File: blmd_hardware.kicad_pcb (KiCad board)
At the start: 2 copper layers, 50 x 28.5 mm, 59 parts, among them J1 MR30PW-F, J2 control, J3 GND, J4 12V, J5 STLink-V3, Q1 RH6L040BG, Q2 RH6L040BG, Q3 RH6L040BG, Q4 RH6L040BG, Q5 RH6L040BG, Q6 RH6L040BG, SW1 reset, SW2 KHS42E, U1 A4939KLPTR-5-T, U10 STM32G431KBTx, U4 ISO7760FDBQR, U6 ACS711KEXLT-31AB, U7 ACS711KEXLT-31AB, U9 BD41041FJ-C

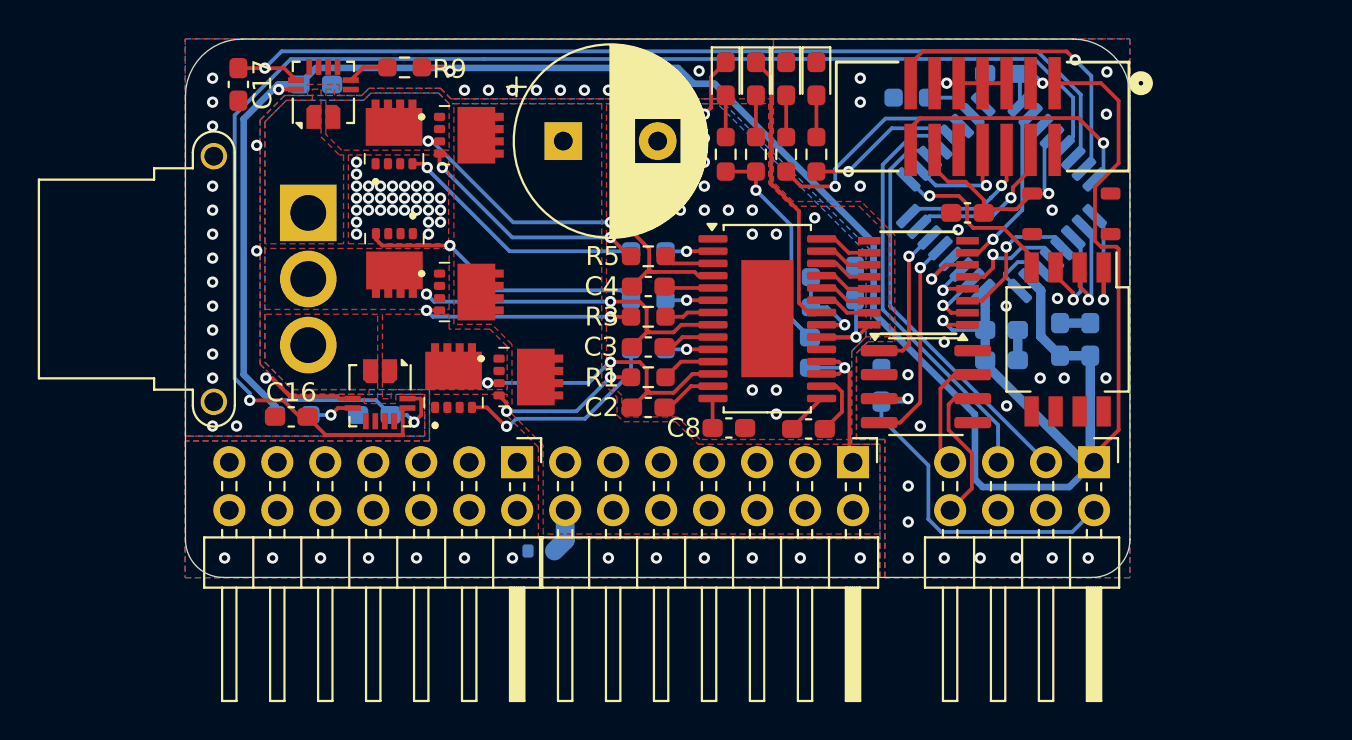
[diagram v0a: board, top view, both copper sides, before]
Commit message: fix : vdd vss position
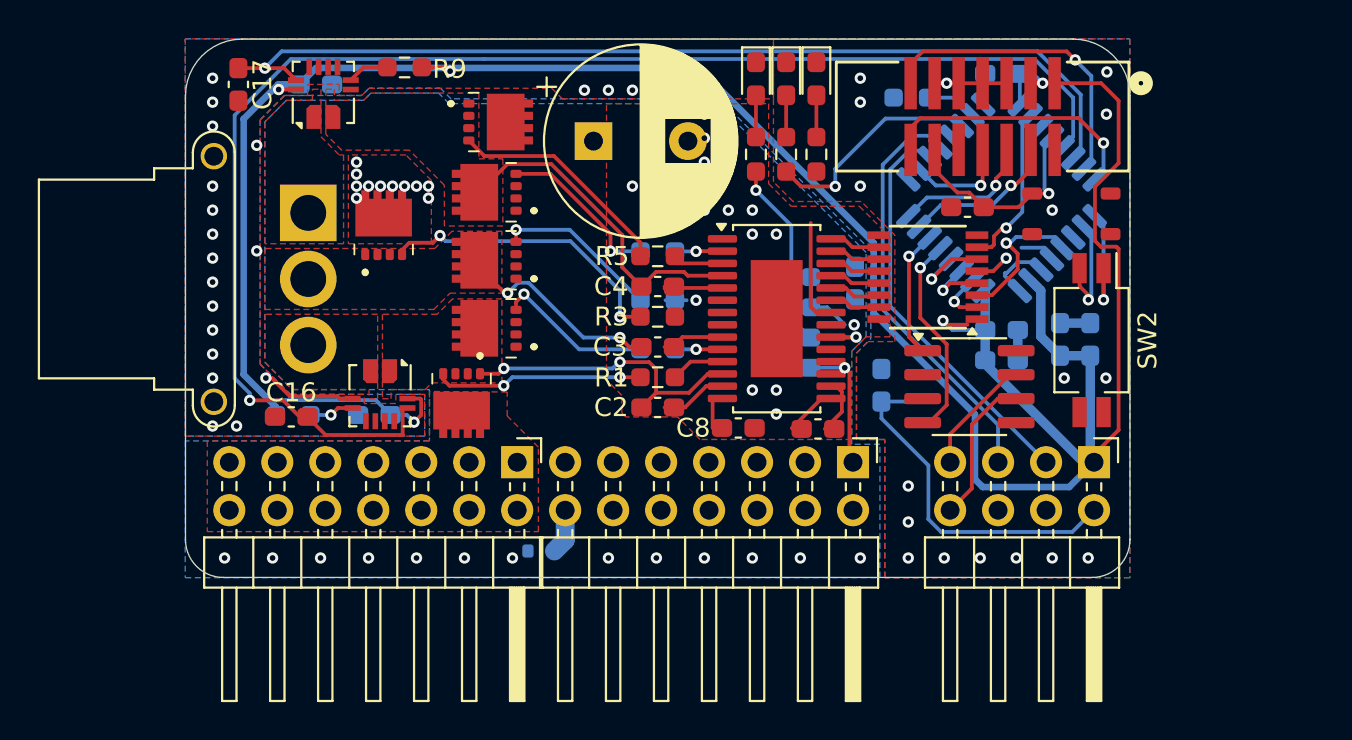
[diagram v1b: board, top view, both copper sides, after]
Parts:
- removed D5: Green, LED_SMD:LED_0603_1608Metric_Pad1.05x0.95mm_HandSolder
- removed R15: 1k, Resistor_SMD:R_0603_1608Metric_Pad0.98x0.95mm_HandSolder
- SW2: value KHS42E -> SW_DIP_x02; footprint Button_Switch_SMD:SW_DIP_SPSTx04_Slide_Copal_CHS-04B_W7.62mm_P1.27mm -> Button_Switch_SMD:SW_DIP_SPSTx02_Slide_Copal_CHS-02B_W7.62mm_P1.27mm
- moved J3 17.8 mm to (85.3, 72.4)
- moved J4 17.8 mm to (67.6, 72.4)
- moved Q2 9.75 mm to (60.5, 57.0), turned to 0 degrees
- moved Q1 7.66 mm to (64.6, 72.1), turned to 180 degrees
- moved Q6 6.25 mm to (63.1, 58.1), turned to 90 degrees
- moved Q5 3.63 mm to (63.1, 61.7), turned to 90 degrees
- moved U9 2.30 mm to (91.5, 68.4)
- moved Q3 1.70 mm to (69.4, 54.4)
- moved D3 1.60 mm to (80.2, 52.1)
- moved D4 1.60 mm to (83.4, 52.1)
- moved R13 1.60 mm to (80.2, 56.1)
- moved R14 1.60 mm to (83.4, 56.1)
- moved C1 1.60 mm to (71.6, 55.4)
- moved D2 1.60 mm to (81.8, 52.1)
- moved R12 1.60 mm to (81.8, 56.1)
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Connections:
- J5 pad 1: +3V3 -> unconnected-(J5-Pin_1-Pad1)
- J5 pad 9: GNDD -> unconnected-(J5-Pin_9-Pad9)
- SW2 pad 3: ID3 -> GNDD
- SW2 pad 4: ID4 -> unconnected-(SW2-Pad4)
- U10 pad 11: ID3 -> unconnected-(U10-PA6-Pad11)
- U10 pad 25: ID4 -> unconnected-(U10-PA15-Pad25)
- U10 pad 29: STATUS -> unconnected-(U10-PB6-Pad29)
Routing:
- net ID4: track 9.96 -> 0.00 mm, vias 1 -> 0
- net Net-(D2-K): track 15.1 -> 5.64 mm
- net STATUS: track 8.27 -> 0.00 mm, vias 1 -> 0
- net HSB: track 18.2 -> 11.2 mm
- net Net-(Q5-G): track 15.1 -> 8.82 mm
- net ID3: track 6.11 -> 0.00 mm, vias 1 -> 0
- net Net-(Q6-G): track 13.5 -> 8.82 mm
- net +5V: track 21.3 -> 16.8 mm
- net Net-(Q2-G): track 11.7 -> 15.8 mm
- net GNDPWR: track 3.36 -> 0.00 mm, vias 61 -> 30
- net HSC: track 20.5 -> 17.6 mm, vias 2 -> 0
- net Net-(Q4-G): track 11.2 -> 8.39 mm
- net Net-(Q1-G): track 8.33 -> 11.1 mm
- net HOB: track 2.61 -> 0.00 mm
- net SIGB_N: track 5.85 -> 3.61 mm
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
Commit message: backup commit
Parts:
- removed the C13 at (85.4, 62.9)
- moved C13 2.72 mm to (89.3, 69.5)
- moved R9 1.70 mm to (63.3, 51.5)
- moved C6 1.50 mm to (83.7, 65.8)
- moved C7 1.50 mm to (83.7, 67.4)
- moved R7 1.50 mm to (83.7, 64.2)
- moved R8 1.50 mm to (83.7, 62.6)
- moved U7 1.19 mm to (58.5, 52.9)
- renumbered C19 to C13
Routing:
- net HSB: track 11.2 -> 15.9 mm
- net ID_DISP: track 11.8 -> 9.03 mm
- net HOB: track 0.00 -> 2.61 mm
- net Net-(U7-~{FAULT}): track 2.22 -> 0.00 mm
- net Net-(U1-VDSTH): track 3.77 -> 5.50 mm
- net +5V: track 16.8 -> 18.5 mm
- net +3V3: track 148.2 -> 146.6 mm, vias 5 -> 4
- net LOB: track 1.12 -> 2.51 mm
- net +5VD: track 18.3 -> 19.1 mm, vias 0 -> 1
- net GNDD: vias 40 -> 39
- net +12VA: vias 12 -> 14

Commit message: backup commit
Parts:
- turned D1 to 0 degrees
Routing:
- net +12VA: track 12.9 -> 25.5 mm, vias 14 -> 40
- net Net-(D2-K): track 5.64 -> 14.7 mm
- net GNDPWR: track 0.00 -> 6.78 mm, vias 30 -> 28
- net Net-(U7-~{FAULT}): track 0.00 -> 2.73 mm
- net +3V3: track 146.6 -> 148.0 mm, vias 4 -> 5
- net Net-(U1-VDSTH): track 5.50 -> 4.20 mm
- net +5V: track 18.5 -> 19.2 mm
- added copper zone on B.Cu, net +12VA

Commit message: tmp : complete?
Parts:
- added R15: 3.3k, Resistor_SMD:R_0603_1608Metric_Pad0.98x0.95mm_HandSolder, B.Cu at (83.7, 52.6)
- added R16: 3.3k, Resistor_SMD:R_0603_1608Metric_Pad0.98x0.95mm_HandSolder, B.Cu at (83.7, 51.0)
- C16, C17: value 0.1u -> 0.01u; moved to B.Cu
- moved C16 45.6 mm to (97.3, 51.6), turned to 0 degrees
- moved C17 45.3 mm to (98.1, 53.3), turned to 0 degrees
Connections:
- J5 pad 1: unconnected-(J5-Pin_1-Pad1) -> +3V3
- J5 pad 13: USART_TX -> unconnected-(J5-Pin_13-Pad13)
- J5 pad 14: USART_RX -> unconnected-(J5-Pin_14-Pad14)
- J5 pad 9: unconnected-(J5-Pin_9-Pad9) -> GNDD
- SW2 pad 4: unconnected-(SW2-Pad4) -> GNDD
- U10 pad 5: SCA -> unconnected-(U10-PA0-Pad5)
- U10 pad 6: SCC -> SCA
- U10 pad 7: USART_TX -> unconnected-(U10-PA2-Pad7)
- U10 pad 8: USART_RX -> SCC
- U6 pad 9: SCA -> Net-(U6-VIOUT)
- U7 pad 9: SCC -> Net-(U7-VIOUT)
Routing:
- net Net-(U6-VIOUT): track 0.00 -> 58.0 mm, vias 0 -> 1
- net SCA: track 75.5 -> 18.0 mm, vias 1 -> 0
- net Net-(U7-VIOUT): track 0.00 -> 32.2 mm, vias 0 -> 1
- net SCC: track 51.3 -> 20.0 mm, vias 1 -> 0
- net USART_TX: track 16.5 -> 0.00 mm, vias 1 -> 0
- net USART_RX: track 14.3 -> 0.00 mm, vias 1 -> 0
- net +12VA: track 25.5 -> 31.4 mm
- net GNDD: track 15.6 -> 12.6 mm, vias 39 -> 36
- net +3V3: track 148.0 -> 149.2 mm
- net unconnected-(J5-Pin_14-Pad14): track 0.00 -> 1.18 mm
- net unconnected-(J5-Pin_13-Pad13): track 0.00 -> 1.04 mm
- net SIGB_N: track 3.61 -> 4.65 mm
- net unconnected-(U10-PA2-Pad7): track 0.00 -> 0.55 mm
- net GNDPWR: vias 28 -> 27

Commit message: backup commit
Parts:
- removed the R11 at (88.4, 53.1)
- added C16: 0.1u, Capacitor_SMD:C_0603_1608Metric_Pad1.08x0.95mm_HandSolder, B.Cu at (108.3, 57.3)
- added R16: 33k, Resistor_SMD:R_0603_1608Metric_Pad0.98x0.95mm_HandSolder, B.Cu at (83.7, 60.6)
- added R17: 33k, Resistor_SMD:R_0603_1608Metric_Pad0.98x0.95mm_HandSolder, B.Cu at (83.5, 58.8)
- added R18: 33k, Resistor_SMD:R_0603_1608Metric_Pad0.98x0.95mm_HandSolder, B.Cu at (83.6, 62.2)
- added R19: 33k, Resistor_SMD:R_0603_1608Metric_Pad0.98x0.95mm_HandSolder, B.Cu at (79.6, 63.9)
- added R20: 33k, Resistor_SMD:R_0603_1608Metric_Pad0.98x0.95mm_HandSolder, B.Cu at (79.6, 62.2)
- added R21: 33k, Resistor_SMD:R_0603_1608Metric_Pad0.98x0.95mm_HandSolder, B.Cu at (79.6, 60.6)
- C15, C6: moved to F.Cu
- Q1, Q2, Q3, Q4, Q5, Q6: value RH6L040BG -> RH6G040CH
- R1, R2, R3, R4, R5, R6: value 39 -> 15
- R9: renamed from R10; moved to F.Cu
- moved C10 15.6 mm to (94.0, 51.4), turned to 180 degrees
- moved C9 14.1 mm to (90.5, 53.0), turned to 180 degrees
- moved C19 11.4 mm to (86.9, 51.0)
- moved C18 10.4 mm to (86.9, 52.6)
- moved C12 8.60 mm to (89.3, 65.9), turned to -90 degrees
- moved C15 3.13 mm to (53.8, 51.7), turned to 180 degrees
- moved C6 2.97 mm to (86.2, 67.4), turned to -90 degrees
- moved R7 1.66 mm to (83.0, 65.7)
- moved R8 1.66 mm to (83.0, 64.1)
- moved U10 1.49 mm to (93.7, 59.8), turned to 45 degrees
- moved C11 1.41 mm to (94.0, 53.0)
- moved C11 1.30 mm to (93.2, 66.7)
- moved C17 0.86 mm to (90.9, 58.2)
- moved C7 0.71 mm to (83.0, 67.3)
- moved R14 0.70 mm to (83.0, 52.6)
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- renumbered C18 to C17, C16 to C18, C17 to C19, R9 to R10, R12 to R11, R13 to R12, R14 to R13, R15 to R14, R16 to R15
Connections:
- J5 pad 1: +3V3 -> unconnected-(J5-Pin_1-Pad1)
- J5 pad 9: GNDD -> unconnected-(J5-Pin_9-Pad9)
- SW2 pad 1: ID1 -> ID2
- SW2 pad 2: ID2 -> ID1
- U10 pad 10: ID2 -> unconnected-(U10-PA5-Pad10)
- U10 pad 11: unconnected-(U10-PA6-Pad11) -> SIGB
- U10 pad 12: SIGA_N -> Net-(U10-PA7)
- U10 pad 13: SIGB_N -> SCC
- U10 pad 19: SIGB -> ID_DISP
- U10 pad 21: RXD -> SIGA_N
- U10 pad 25: unconnected-(U10-PA15-Pad25) -> ID2
- U10 pad 29: unconnected-(U10-PB6-Pad29) -> SIGB_N
- U10 pad 3: unconnected-(U10-PF1-Pad3) -> REF0
- U10 pad 30: ID_DISP -> ID1
- U10 pad 31: Net-(U10-PB8) -> RXD
- U10 pad 5: unconnected-(U10-PA0-Pad5) -> Net-(U10-PA0)
- U10 pad 6: SCA -> Net-(U10-PA1)
- U10 pad 7: unconnected-(U10-PA2-Pad7) -> REF0
- U10 pad 8: SCC -> SCA
- U10 pad 9: ID1 -> REF0
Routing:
- net GNDD: track 12.6 -> 0.00 mm, vias 36 -> 29
- net SPD2: track 22.2 -> 12.1 mm
- net TXD: track 6.81 -> 16.8 mm, vias 1 -> 2
- net SCC: track 20.0 -> 10.1 mm
- net SPD1: track 21.6 -> 11.7 mm
- net SIGA: track 2.85 -> 12.7 mm
- net +3V3: track 149.2 -> 140.7 mm, vias 5 -> 7
- net ID_DISP: track 9.03 -> 15.9 mm, vias 1 -> 2
- net SCA: track 18.0 -> 11.4 mm, vias 0 -> 2
- net SIGC: track 4.33 -> 8.98 mm
- net SIGB: track 3.47 -> 7.65 mm
- net +12VA: track 31.4 -> 27.5 mm
- net Net-(U7-VIOUT): track 32.2 -> 28.4 mm, vias 1 -> 2
- net REF0: track 0.00 -> 3.62 mm
- net SIGC_N: track 8.93 -> 5.39 mm
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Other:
- copper layers 2 -> 4

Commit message: back up commit
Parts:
- removed the C6 at (86.2, 67.4)
- removed the C7 at (83.0, 67.3)
- removed the C8 at (79.3, 70.6)
- removed the R17 at (83.5, 58.8)
- removed the R7 at (83.0, 65.7)
- removed the R8 at (83.0, 64.1)
- removed U10: STM32G431KBTx, Package_QFP:LQFP-32_7x7mm_P0.8mm
- removed the U4 at (89.3, 62.6)
- removed U9: BD41041FJ-C, Package_SO:SOIC-8_3.9x4.9mm_P1.27mm
- added C10: 10u, Capacitor_SMD:C_0603_1608Metric_Pad1.08x0.95mm_HandSolder, B.Cu at (73.6, 52.9)
- added C17: 0.1u, Capacitor_SMD:C_0603_1608Metric_Pad1.08x0.95mm_HandSolder, B.Cu at (89.7, 70.3)
- added D3: schot, Diode_SMD:D_SOD-323F, B.Cu at (71.0, 64.8)
- added D4: schot, Diode_SMD:D_SOD-323F, B.Cu at (71.0, 61.8)
- added D5: fast rec, Diode_SMD:D_SOD-323F, F.Cu at (81.5, 69.7)
- added D7: Green, LED_SMD:LED_0603_1608Metric_Pad1.05x0.95mm_HandSolder, F.Cu at (90.5, 51.6)
- added J6: GH4, Connector_JST:JST_GH_SM04B-GHS-TB_1x04-1MP_P1.25mm_Horizontal, F.Cu at (83.5, 52.9)
- added L1: 2.2u, Inductor_SMD:L_0603_1608Metric_Pad1.05x0.95mm_HandSolder, F.Cu at (85.3, 69.7)
- added R10: 33k, Resistor_SMD:R_0603_1608Metric_Pad0.98x0.95mm_HandSolder, B.Cu at (76.4, 63.1)
- added R12: 33k, Resistor_SMD:R_0603_1608Metric_Pad0.98x0.95mm_HandSolder, B.Cu at (76.4, 69.3)
- added R19: 22k, Resistor_SMD:R_0603_1608Metric_Pad0.98x0.95mm_HandSolder, B.Cu at (89.8, 55.1)
- added R20: 1.2k, Resistor_SMD:R_0603_1608Metric_Pad0.98x0.95mm_HandSolder, B.Cu at (82.0, 67.8)
- added R21: 10k, Resistor_SMD:R_0603_1608Metric_Pad0.98x0.95mm_HandSolder, B.Cu at (82.0, 70.1)
- added R24: 10k, Resistor_SMD:R_0603_1608Metric_Pad0.98x0.95mm_HandSolder, B.Cu at (85.7, 69.9)
- added U2: ISO6520, Package_SO:SOIC-8_3.9x4.9mm_P1.27mm, F.Cu at (96.2, 68.7)
- added U3: TCAN3414DDFR, Package_TO_SOT_SMD:SOT-23-8, F.Cu at (91.1, 63.5)
- C1: value 470u -> 330u
- C11: value 0.1u -> 10u
- C12, C13, C14: moved to F.Cu
- C18: renamed from C17; moved to B.Cu
- C19: renamed from C11; moved to F.Cu
- C5: value 0.47u -> 22u; footprint Capacitor_SMD:C_0603_1608Metric_Pad1.08x0.95mm_HandSolder -> Capacitor_SMD:C_0805_2012Metric_Pad1.18x1.45mm_HandSolder
- D1: value TVS -> schot; footprint Diode_SMD:D_SOD-523 -> Diode_SMD:D_SOD-323F; moved to F.Cu
- D2: value blue -> schot; footprint LED_SMD:LED_0603_1608Metric_Pad1.05x0.95mm_HandSolder -> Diode_SMD:D_SOD-323F; moved to B.Cu
- R11: value 2.2k -> 33k; moved to B.Cu
- R15: renamed from R12; value 2.2k -> 5k
- R16: value 33k -> 1k; moved to F.Cu
- R18: value 33k -> 6.8k
- SW1, SW2: moved to B.Cu
- U1: value A4939KLPTR-5-T -> STSPIN32G4; footprint Package_SO:HTSSOP-28-1EP_4.4x9.7mm_P0.65mm_EP2.75x6.2mm -> blmd_hardware:QFN_IN32G4_STM
- moved D1 28.8 mm to (91.2, 58.9), turned to 90 degrees
- moved C16 19.3 mm to (94.1, 70.3)
- moved D2 19.2 mm to (71.0, 68.0), turned to 180 degrees
- moved C8 15.5 mm to (80.1, 58.4)
- moved C19 13.4 mm to (81.3, 57.4)
- moved R11 11.5 mm to (76.4, 66.2), turned to 180 degrees
- moved C9 11.0 mm to (80.1, 56.8)
- moved R18 10.5 mm to (91.3, 55.1), turned to 90 degrees
- moved R23 9.30 mm to (54.0, 51.3), turned to 180 degrees
- moved R15 8.80 mm to (89.0, 55.1)
- moved D6 8.76 mm to (89.0, 51.6)
- moved R17 8.70 mm to (92.0, 55.1)
- moved R16 8.69 mm to (90.5, 55.1), turned to 90 degrees
- moved D8 8.66 mm to (92.0, 51.6)
- moved C18 8.60 mm to (97.6, 52.9), turned to 0 degrees
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- renumbered C18 to C6, C19 to C7, C10 to C8, D3 to D6, D4 to D8, R14 to R13, R15 to R14, R13 to R17, R9 to R22, R10 to R23, R19 to R7, R20 to R8, R21 to R9, U6 to U4, U7 to U5
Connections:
- C1 pad 2: GNDPWR -> GND
- C11 pad 2: GNDD -> GND
- C12 pad 2: GNDD -> GND
- C13 pad 1: +5VD -> +3V3
- C13 pad 2: GNDD -> GND
- C14 pad 2: GNDD -> GND
- C15 pad 2: GNDD -> GND
- C16 pad 1: +5V -> +3.3V
- C16 pad 2: GNDPWR -> GNDD
- C18 pad 2: GNDD -> GND
- C19 pad 2: GNDD -> GND
- C2 pad 2: Net-(U1-CA) -> BOOTA
- C3 pad 1: HSB -> BOOTB
- C3 pad 2: Net-(U1-CB) -> HSB
- C4 pad 1: HSC -> BOOTC
- C4 pad 2: Net-(U1-CC) -> HSC
- C5 pad 1: Net-(U1-CP1) -> +12V
- C5 pad 2: Net-(U1-CP2) -> GND
- C6 pad 2: GNDD -> GND
- C7 pad 2: GNDD -> GND
- C8 pad 2: GNDD -> GND
- C9 pad 2: GNDD -> GND
- D1 pad 1: +12VA -> +3V3
- D1 pad 2: GNDPWR -> MON
- D2 pad 1: Net-(D2-K) -> BOOTA
- D2 pad 2: Net-(D2-A) -> +12V
- D6 pad 1: GNDPWR -> GND
- D8 pad 1: GNDD -> GND
- J2 pad 1: +3V3 -> +3.3V
- J3 pad 1: GNDPWR -> GND
- J3 pad 10: GNDPWR -> GND
- J3 pad 11: GNDPWR -> GND
- J3 pad 12: GNDPWR -> GND
- J3 pad 13: GNDPWR -> GND
- J3 pad 14: GNDPWR -> GND
- J3 pad 2: GNDPWR -> GND
- J3 pad 3: GNDPWR -> GND
- J3 pad 4: GNDPWR -> GND
- J3 pad 5: GNDPWR -> GND
- J3 pad 6: GNDPWR -> GND
- J3 pad 7: GNDPWR -> GND
- J3 pad 8: GNDPWR -> GND
- J3 pad 9: GNDPWR -> GND
- J5 pad 11: GNDD -> GND
- J5 pad 13: unconnected-(J5-Pin_13-Pad13) -> USART_TX
- J5 pad 14: unconnected-(J5-Pin_14-Pad14) -> USART_RX
- J5 pad 5: GNDD -> GND
- J5 pad 7: GNDD -> GND
- Q4 pad 1: GNDPWR -> GND
- Q4 pad 2: GNDPWR -> GND
- Q4 pad 3: GNDPWR -> GND
- Q5 pad 1: GNDPWR -> GND
- Q5 pad 2: GNDPWR -> GND
- Q5 pad 3: GNDPWR -> GND
- Q6 pad 1: GNDPWR -> GND
- Q6 pad 2: GNDPWR -> GND
- Q6 pad 3: GNDPWR -> GND
- R11 pad 1: Net-(D2-A) -> Net-(U1-PA7)
- R11 pad 2: +5V -> HSB
- R15 pad 1: +5V -> +12V
- R16 pad 1: Net-(U10-PA1) -> STATUS
- R16 pad 2: HSA -> Net-(D7-A)
- R18 pad 1: Net-(U10-PA0) -> MON
- R18 pad 2: HSC -> GND
- SW1 pad 1: GNDD -> GND
- SW2 pad 3: GNDD -> GND
- SW2 pad 4: GNDD -> GND
- U1 pad 1: GNDPWR -> +3V3
- U1 pad 10: LOA -> Net-(U1-PC1)
- U1 pad 11: HOA -> SIN
- U1 pad 12: HSA -> COS
- U1 pad 13: Net-(U1-CA) -> unconnected-(U1-PA0-Pad13)
- U1 pad 14: Net-(U1-VREG) -> SCC
- U1 pad 15: Net-(U1-CP2) -> unconnected-(U1-PA2-Pad15)
- U1 pad 16: Net-(U1-CP1) -> MON
- U1 pad 17: +12VA -> REF0
- U1 pad 18: +12VA -> REF0
- U1 pad 19: GNDPWR -> unconnected-(U1-PA6-Pad19)
- U1 pad 2: LOC -> +3V3
- U1 pad 20: +5V -> Net-(U1-PA7)
- U1 pad 21: Net-(U1-VDSTH) -> unconnected-(U1-PC4-Pad21)
- U1 pad 22: Net-(D2-K) -> unconnected-(U1-PC5-Pad22)
- U1 pad 23: PWMA -> SCA
- U1 pad 24: PWMA_N -> Net-(U1-PB1)
- U1 pad 25: PWMB -> unconnected-(U1-PB2-Pad25)
- U1 pad 26: PWMB_N -> +3V3
- U1 pad 27: PWMC -> +3V3
- U1 pad 28: PWMC_N -> unconnected-(U1-PB10-Pad28)
- U1 pad 29: GNDPWR -> LOA
- U1 pad 3: HOC -> unconnected-(U1-PC13-Pad3)
- U1 pad 4: HSC -> unconnected-(U1-PC14/OCC_IN-Pad4)
- U1 pad 5: Net-(U1-CC) -> unconnected-(U1-PC15/OCC_OUT-Pad5)
- U1 pad 6: LOB -> unconnected-(U1-PF0/OCC_IN-Pad6)
- U1 pad 7: HOB -> unconnected-(U1-PF1/OCC_OUT-Pad7)
- U1 pad 8: HSB -> NRST
- U1 pad 9: Net-(U1-CB) -> REF0
- U4 pad 3: GNDD -> GND
- U5 pad 3: GNDD -> GND
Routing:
- net +3V3: track 140.7 -> 11.4 mm, vias 7 -> 3
- net Net-(U4-VIOUT): track 56.4 -> 1.83 mm, vias 2 -> 1
- net USART_TX: track 0.00 -> 28.5 mm, vias 0 -> 2
- net Net-(U5-VIOUT): track 28.4 -> 0.00 mm, vias 2 -> 0
- net +12VA: track 27.5 -> 0.79 mm, vias 40 -> 24
- net USART_RX: track 0.00 -> 25.2 mm, vias 0 -> 2
- net REF0: track 3.62 -> 26.4 mm, vias 0 -> 1
- net +5V: track 20.8 -> 0.00 mm, vias 2 -> 0
- net +5VD: track 19.1 -> 0.00 mm, vias 1 -> 0
- net SWDIO: track 5.88 -> 23.5 mm, vias 1 -> 2
- net SPD1_O: track 0.00 -> 16.0 mm, vias 0 -> 2
- net SPD2_O: track 0.00 -> 15.3 mm, vias 0 -> 2
- net LOA: track 2.51 -> 17.7 mm
- net Net-(D2-K): track 14.8 -> 0.00 mm
- net Net-(U1-PC1): track 0.00 -> 14.7 mm, vias 0 -> 1
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- added copper zone on B.Cu, net GND
- added copper zone on F.Cu, net GND
- removed copper zone on B.Cu, net GNDD
- removed copper zone on F.Cu, net GNDD
- removed copper zone on B.Cu, net GNDPWR
- removed copper zone on F.Cu, net GNDPWR

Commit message: tmp : complete
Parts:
- C8, R18: moved to F.Cu
- moved C7 25.6 mm to (61.3, 51.1)
- moved R14 25.3 mm to (57.7, 51.1)
- moved C6 22.6 mm to (73.2, 70.5)
- moved R13 22.4 mm to (69.5, 70.5)
- moved C10 19.6 mm to (87.4, 66.8)
- moved C8 4.38 mm to (84.3, 57.1), turned to 0 degrees
- moved R18 4.24 mm to (89.8, 59.1), turned to -90 degrees
- moved C19 0.82 mm to (80.5, 57.1)
- moved D1 0.42 mm to (91.6, 59.1)
- moved R19 0.37 mm to (89.4, 55.2)
- moved C11 0.30 mm to (90.8, 67.6)
- moved C9 0.23 mm to (80.3, 56.9)
- moved C18 0.08 mm to (97.7, 52.8)
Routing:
- net +3V3: track 11.4 -> 164.9 mm, vias 3 -> 8
- net +12V: track 11.3 -> 51.6 mm, vias 0 -> 3
- net +12VA: track 0.79 -> 40.7 mm, vias 24 -> 56
- net SCC: track 5.54 -> 35.4 mm, vias 1 -> 2
- net STATUS: track 1.16 -> 28.5 mm, vias 1 -> 2
- net SCA: track 2.12 -> 21.3 mm, vias 0 -> 2
- net GNDD: track 0.00 -> 19.0 mm, vias 0 -> 1
- net ID_DISP: track 3.27 -> 20.7 mm, vias 1 -> 2
- net GND: track 0.27 -> 13.4 mm, vias 13 -> 110
- net Net-(U4-VIOUT): track 1.83 -> 11.0 mm, vias 1 -> 2
- net NRST: track 15.3 -> 23.5 mm
- net MON: track 0.77 -> 8.16 mm, vias 1 -> 2
- net +3.3V: track 3.64 -> 7.70 mm
- net Net-(U5-VIOUT): track 0.00 -> 2.10 mm, vias 0 -> 1
- net Net-(U1-PA7): track 12.2 -> 12.7 mm
- added copper zone on In1.Cu, net GND
- added copper zone on In2.Cu, net GND
